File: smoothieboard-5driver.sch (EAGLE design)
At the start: 253 parts, among them IC1 LPC1769, IC10 LM1117-3.3V, IC11 78L12F, IC12 A4982, IC2 A4982, IC3 A4982, IC4 MCP44X1, IC5 A4982, IC6 A4982, IC9 MCP44X1, J10 POWER_JACKSMD, Q1 BSL207SP, Q2 12MHz, Q3 25MHz, Q6 AOT240L, Q7 AOT240L, Q8 ZXMN4A06GTA, Q9 ZXMN4A06GTA, U1 USD-SOCKETNEW, X14 USBPTH

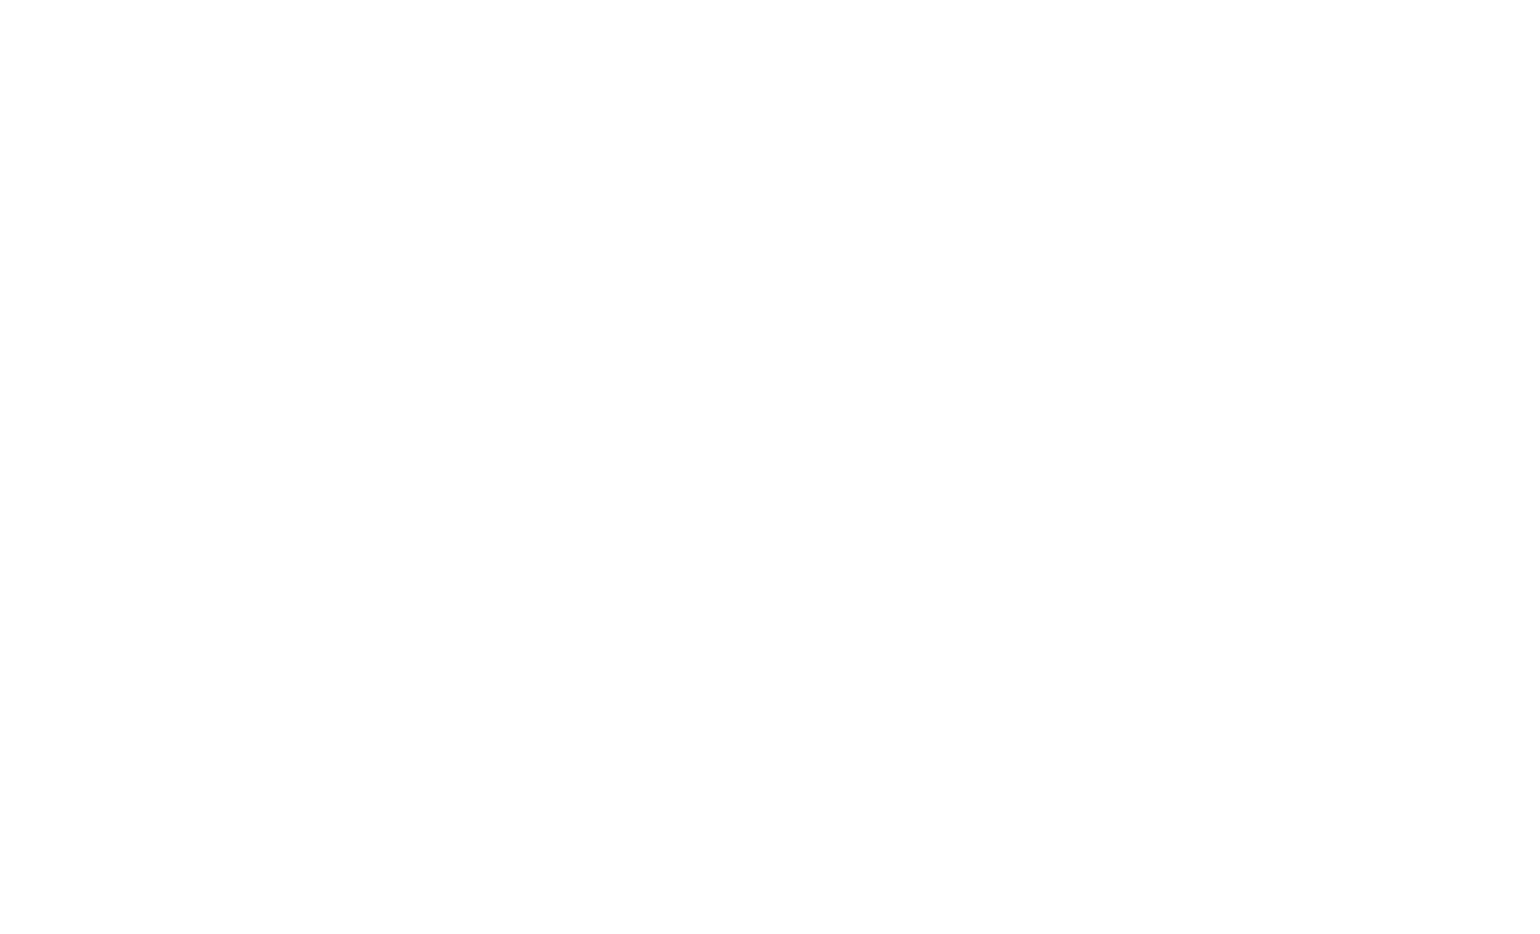
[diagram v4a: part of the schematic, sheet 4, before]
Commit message: Initial placement of extra mosfets
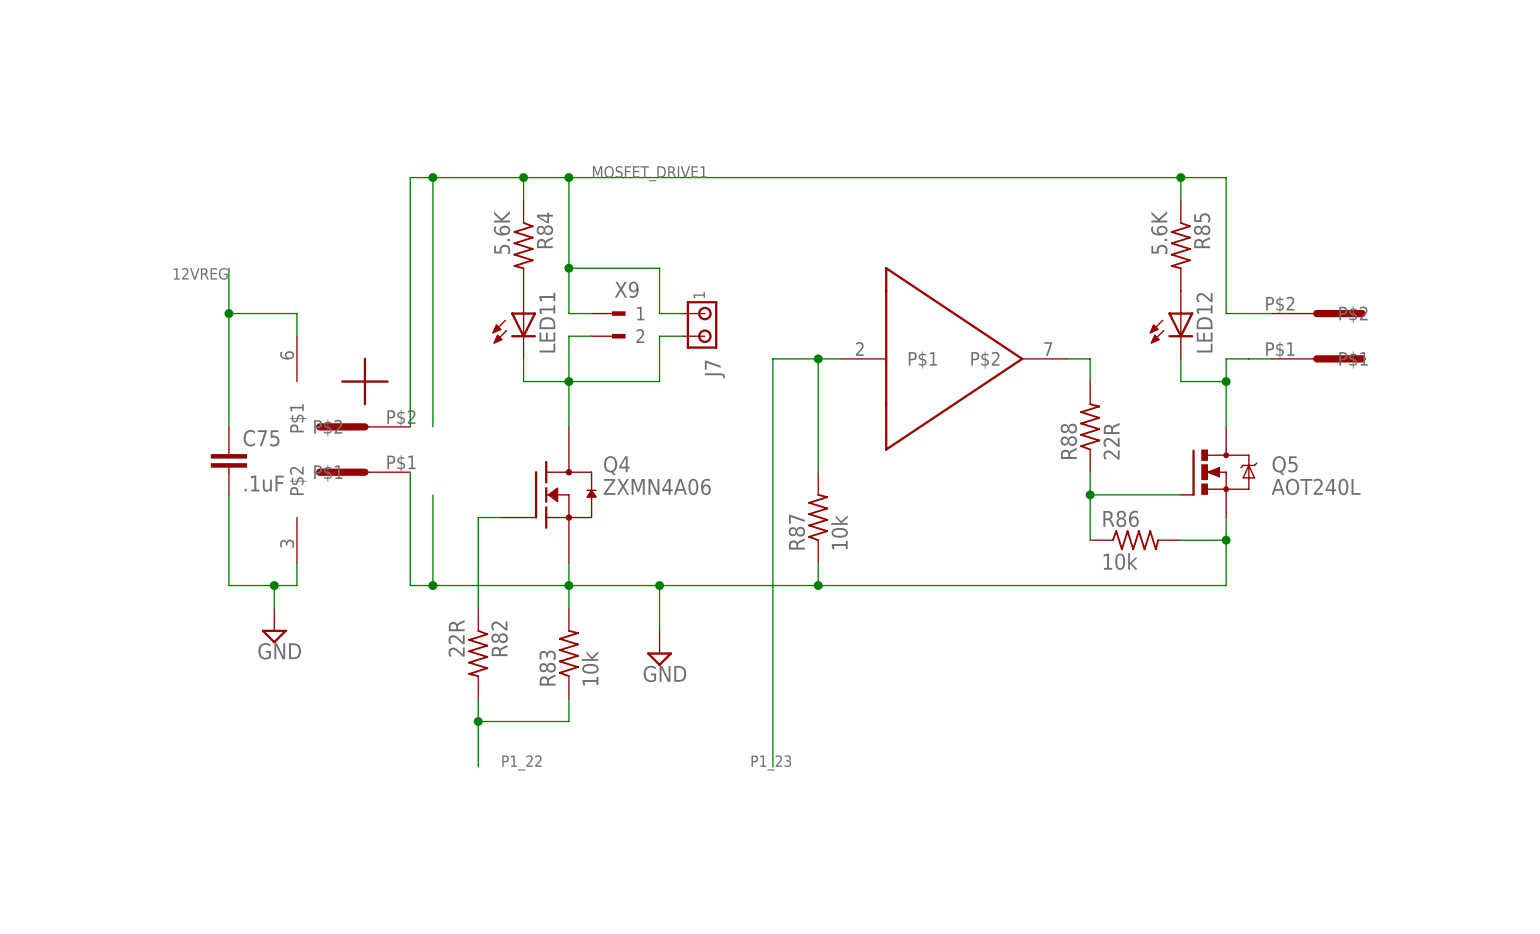
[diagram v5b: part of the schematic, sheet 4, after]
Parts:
- added C75: .1uF, resistor:C-EUC0603
- added J7: (no value), con-amp:MTA02-100
- added LED11, LED12: (no value), led:LEDCHIP-LED0805
- added Q4: ZXMN4A06, ipc-7351-transistor:MOSFET-NCH_SOT-223
- added Q5: AOT240L, transistor-power:IRF540
- added R82, R88: 22R, resistor:R-US_R0603
- added R83, R86, R87: 10k, resistor:R-US_R0603
- added R84, R85: 5.6K, resistor:R-US_R0603
- added U$7, U$9: 5MMCONN, eric_sorensen:5MMCONN
- added U$8: TC4427, custom_esorensen:TC4427
- added X9: (no value), con-weidmueller-sl35:180G-2
- Q8, Q9: value ZXMN4A06GTA -> ZXMN4A06
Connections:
- new net GPIO_FET1: Q5.G, R86.1, R88.1
- new net MOSFET_DRIVE1: J7.1, R84.1, R85.1, U$7.P$2, U$9.P$2, X9.1
- new net N$100: LED11.A, R84.2
- new net N$109: LED12.C, Q5.D, U$7.P$1
- new net N$110: LED12.A, R85.2
- new net N$113: R88.2, U$8A.P$2
- new net N$52: J7.2, LED11.C, Q4.D, X9.2
- new net N$97: Q4.G, R82.1
- net 12VREG: now also C75.1, U$8RAILS.P$1
- net GND: now also C75.2, Q4.S, Q5.S, R83.2, R86.2, R87.1, U$8RAILS.P$2, U$9.P$1
- net P1_22: now also R82.2, R83.1
- net P1_23: now also R87.2, U$8A.P$1

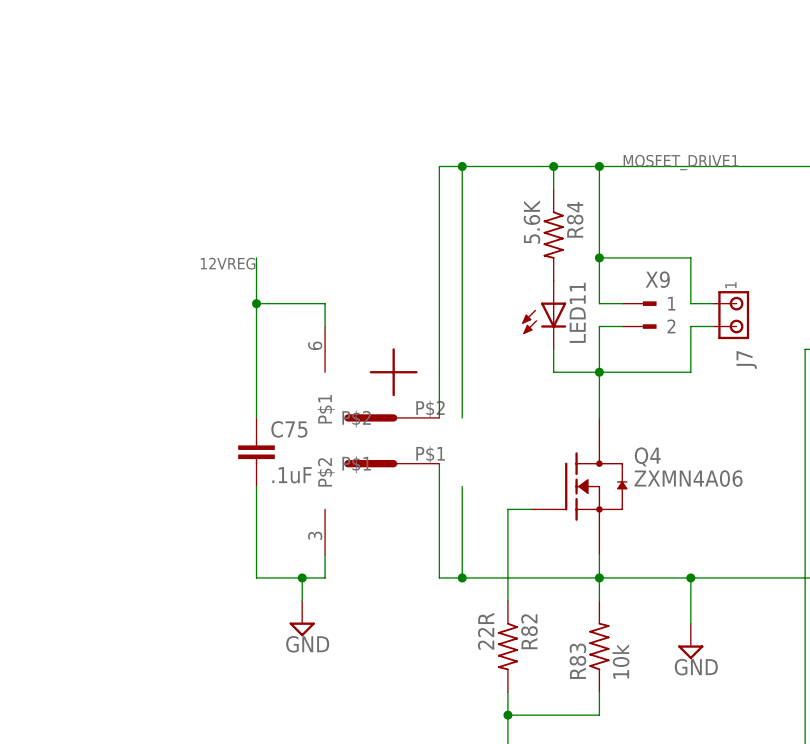
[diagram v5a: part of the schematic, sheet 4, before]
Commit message: Extra mosfets routed
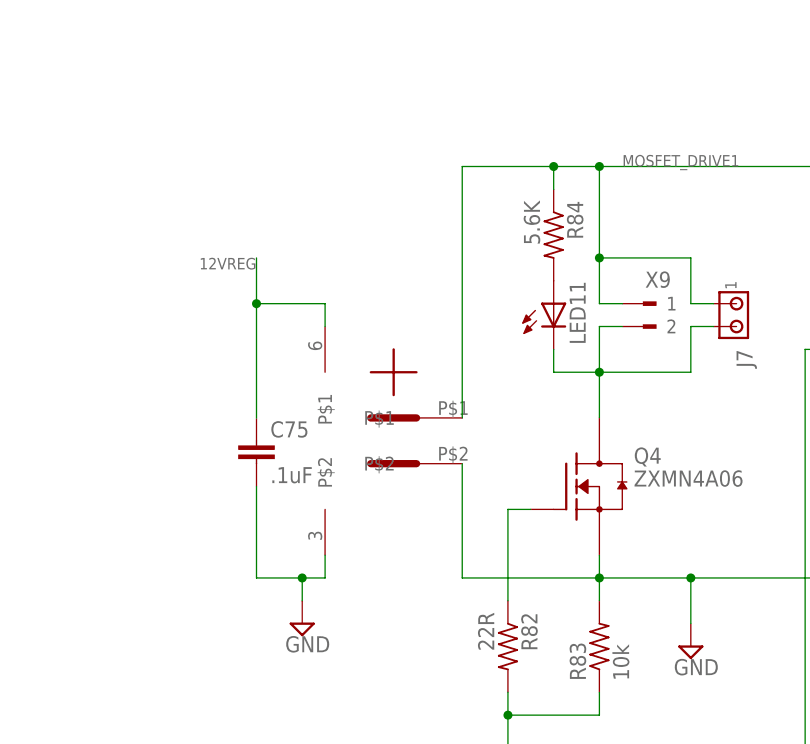
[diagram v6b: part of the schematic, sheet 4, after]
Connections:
- net GND: now also U$9.P$2; no longer U$9.P$1
- net MOSFET_DRIVE1: now also U$9.P$1; no longer U$9.P$2
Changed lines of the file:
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@@
 <setting verticaltext="up"/>
 </settings>
-<grid distance="100" unitdist="mil" unit="mil" style="lines" multiple="1" display="no" altdistance="0.01" altunitdist="inch" altunit="inch"/>
+<grid distance="0.1" unitdist="inch" unit="inch" style="lines" multiple="1" display="no" altdistance="0.01" altunitdist="inch" altunit="inch"/>
 <layers>
 <layer number="1" name="Top" color="4" fill="1" visible="no" active="no"/>
@@
 <instance part="SUPPLY83" gate="GND" x="167.64" y="167.64"/>
 <instance part="R87" gate="G$1" x="228.6" y="180.34" rot="R90"/>
-<instance part="U$9" gate="G$1" x="177.8" y="190.5" rot="R180"/>
+<instance part="U$9" gate="G$1" x="180.34" y="185.42" rot="MR0"/>
 <instance part="R88" gate="G$1" x="259.08" y="190.5" rot="R90"/>
 </instances>
@@
 <pinref part="R87" gate="G$1" pin="1"/>
 <wire x1="228.6" y1="175.26" x2="228.6" y2="172.72" width="0.1524" layer="91"/>
-<wire x1="185.42" y1="172.72" x2="185.42" y2="182.88" width="0.1524" layer="91"/>
-<pinref part="U$9" gate="G$1" pin="P$1"/>
-<wire x1="185.42" y1="172.72" x2="182.88" y2="172.72" width="0.1524" layer="91"/>
-<wire x1="182.88" y1="172.72" x2="182.88" y2="185.42" width="0.1524" layer="91"/>
-<junction x="185.42" y="172.72"/>
+<wire x1="185.42" y1="172.72" x2="185.42" y2="185.42" width="0.1524" layer="91"/>
 <wire x1="228.6" y1="172.72" x2="274.32" y2="172.72" width="0.4064" layer="91"/>
 <wire x1="274.32" y1="172.72" x2="274.32" y2="177.8" width="0.4064" layer="91"/>
@@
 <junction x="274.32" y="177.8"/>
 <junction x="228.6" y="172.72"/>
+<pinref part="U$9" gate="G$1" pin="P$2"/>
 </segment>
 <segment>
@@
 <junction x="200.66" y="218.44"/>
 <wire x1="185.42" y1="218.44" x2="185.42" y2="190.5" width="0.1524" layer="91"/>
-<pinref part="U$9" gate="G$1" pin="P$2"/>
-<wire x1="185.42" y1="218.44" x2="182.88" y2="218.44" width="0.1524" layer="91"/>
-<wire x1="182.88" y1="218.44" x2="182.88" y2="190.5" width="0.1524" layer="91"/>
-<junction x="185.42" y="218.44"/>
+<pinref part="U$9" gate="G$1" pin="P$1"/>
 </segment>
 </net>

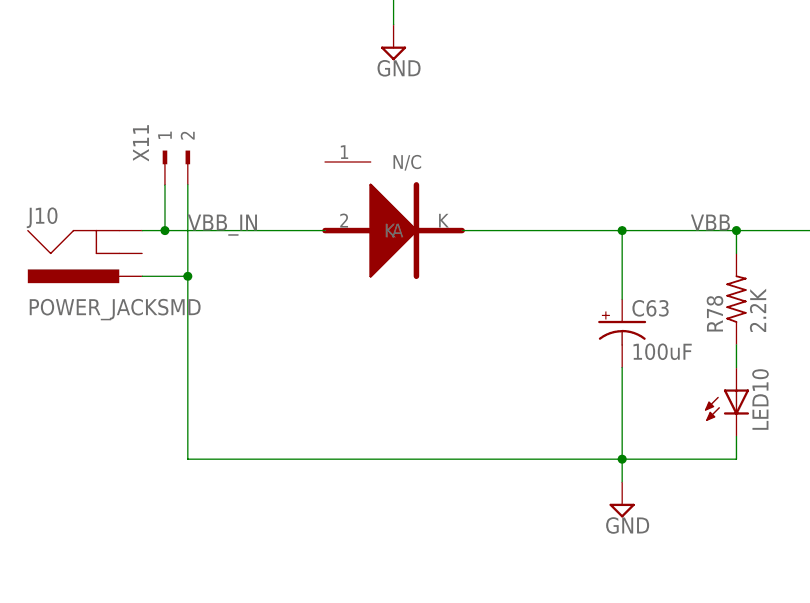
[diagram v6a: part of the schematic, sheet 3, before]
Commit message: Change type of primary diode to a more robust type with lower Vf, add a helper diode to prevent damage from primary diode's higher reverse leakage
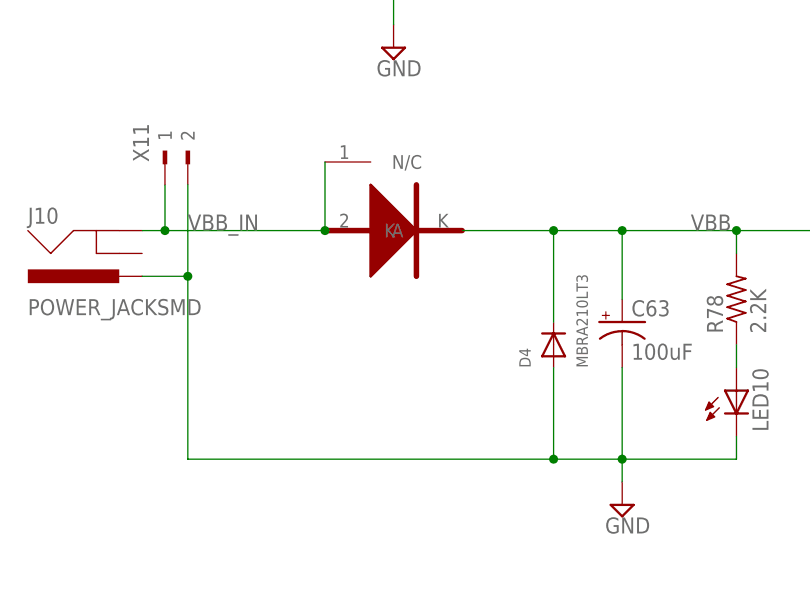
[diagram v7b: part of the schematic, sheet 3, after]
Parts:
- added D4: MBRA210LT3, microbuilder:DIODESMA
- D3: value (none) -> VS-25CTQ045S
- renumbered U$1 to D3
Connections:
- net GND: now also D4.A
- net VBB: now also D4.C
- net VBB_IN: now also D3.N/C
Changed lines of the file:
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@@
 <part name="X10" library="con-weidmueller-sl35" deviceset="180G-2" device=""/>
 <part name="X6" library="con-weidmueller-sl35" deviceset="180G-2" device=""/>
-<part name="U$1" library="Geos" deviceset="ETH1506S" device=""/>
+<part name="D3" library="Geos" deviceset="ETH1506S" device="" value="VS-25CTQ045S"/>
 <part name="JP28" library="jumper" deviceset="JP1E" device=""/>
 <part name="JP11" library="jumper" deviceset="JP1E" device=""/>
@@
 <part name="U$9" library="eric_sorensen" deviceset="5MMCONN" device=""/>
 <part name="R88" library="resistor" deviceset="R-US_" device="R0603" value="22R"/>
+<part name="D4" library="microbuilder" deviceset="DIODE" device="SMA" value="MBRA210LT3"/>
 </parts>
 <sheets>
@@
 <instance part="X10" gate="G$1" x="304.8" y="88.9" rot="MR180"/>
 <instance part="X6" gate="G$1" x="223.52" y="127" rot="R90"/>
-<instance part="U$1" gate="G$1" x="144.78" y="45.72" rot="R270"/>
+<instance part="D3" gate="G$1" x="144.78" y="45.72" rot="R270"/>
 <instance part="JP28" gate="A" x="254" y="129.54"/>
 <instance part="JP11" gate="A" x="312.42" y="137.16"/>
@@
 <instance part="U$5" gate="G$1" x="284.48" y="132.08" rot="R90"/>
 <instance part="U$6" gate="G$1" x="340.36" y="91.44" rot="MR180"/>
+<instance part="D4" gate="G$1" x="167.64" y="30.48" rot="R90"/>
 </instances>
 <busses>
@@
 <wire x1="121.92" y1="38.1" x2="127" y2="38.1" width="0.1524" layer="91"/>
 <wire x1="127" y1="38.1" x2="127" y2="17.78" width="0.1524" layer="91"/>
-<wire x1="175.26" y1="17.78" x2="127" y2="17.78" width="0.1524" layer="91"/>
+<wire x1="175.26" y1="17.78" x2="167.64" y2="17.78" width="0.1524" layer="91"/>
+<wire x1="167.64" y1="17.78" x2="127" y2="17.78" width="0.1524" layer="91"/>
 <wire x1="127" y1="48.26" x2="127" y2="38.1" width="0.1524" layer="91"/>
 <junction x="175.26" y="17.78"/>
@@
 <pinref part="J10" gate="G$1" pin="PWR"/>
 <pinref part="X11" gate="G$1" pin="2"/>
+<pinref part="D4" gate="G$1" pin="A"/>
+<wire x1="167.64" y1="27.94" x2="167.64" y2="17.78" width="0.1524" layer="91"/>
+<junction x="167.64" y="17.78"/>
 </segment>
 <segment>
@@
 <wire x1="187.96" y1="43.18" x2="205.74" y2="43.18" width="0.1524" layer="91"/>
 <wire x1="175.26" y1="35.56" x2="175.26" y2="43.18" width="0.1524" layer="91"/>
-<wire x1="157.48" y1="43.18" x2="175.26" y2="43.18" width="0.1524" layer="91"/>
+<wire x1="157.48" y1="43.18" x2="167.64" y2="43.18" width="0.1524" layer="91"/>
+<wire x1="167.64" y1="43.18" x2="175.26" y2="43.18" width="0.1524" layer="91"/>
 <wire x1="187.96" y1="40.64" x2="187.96" y2="43.18" width="0.1524" layer="91"/>
 <junction x="175.26" y="43.18"/>
@@
 <pinref part="R78" gate="G$1" pin="2"/>
 <pinref part="C63" gate="G$1" pin="+"/>
-<pinref part="U$1" gate="G$1" pin="K"/>
+<pinref part="D3" gate="G$1" pin="K"/>
+<pinref part="D4" gate="G$1" pin="C"/>
+<wire x1="167.64" y1="33.02" x2="167.64" y2="43.18" width="0.1524" layer="91"/>
+<junction x="167.64" y="43.18"/>
 </segment>
 <segment>
@@
 <pinref part="J10" gate="G$1" pin="GND"/>
 <pinref part="X11" gate="G$1" pin="1"/>
-<pinref part="U$1" gate="G$1" pin="A"/>
+<pinref part="D3" gate="G$1" pin="A"/>
+<pinref part="D3" gate="G$1" pin="N/C"/>
+<wire x1="142.24" y1="43.18" x2="142.24" y2="50.8" width="0.1524" layer="91"/>
+<junction x="142.24" y="43.18"/>
 </segment>
 <segment>
